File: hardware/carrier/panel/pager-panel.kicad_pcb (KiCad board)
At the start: 2 copper layers, 40 x 20 mm, 27 parts, among them J1 GDEY029T94 FPC, J2 CARRIER, J3 FL-A FPC (FL03), J4 FL-B FPC (Orient), J5 FRONTLIGHT, Q5 SI1308EDL

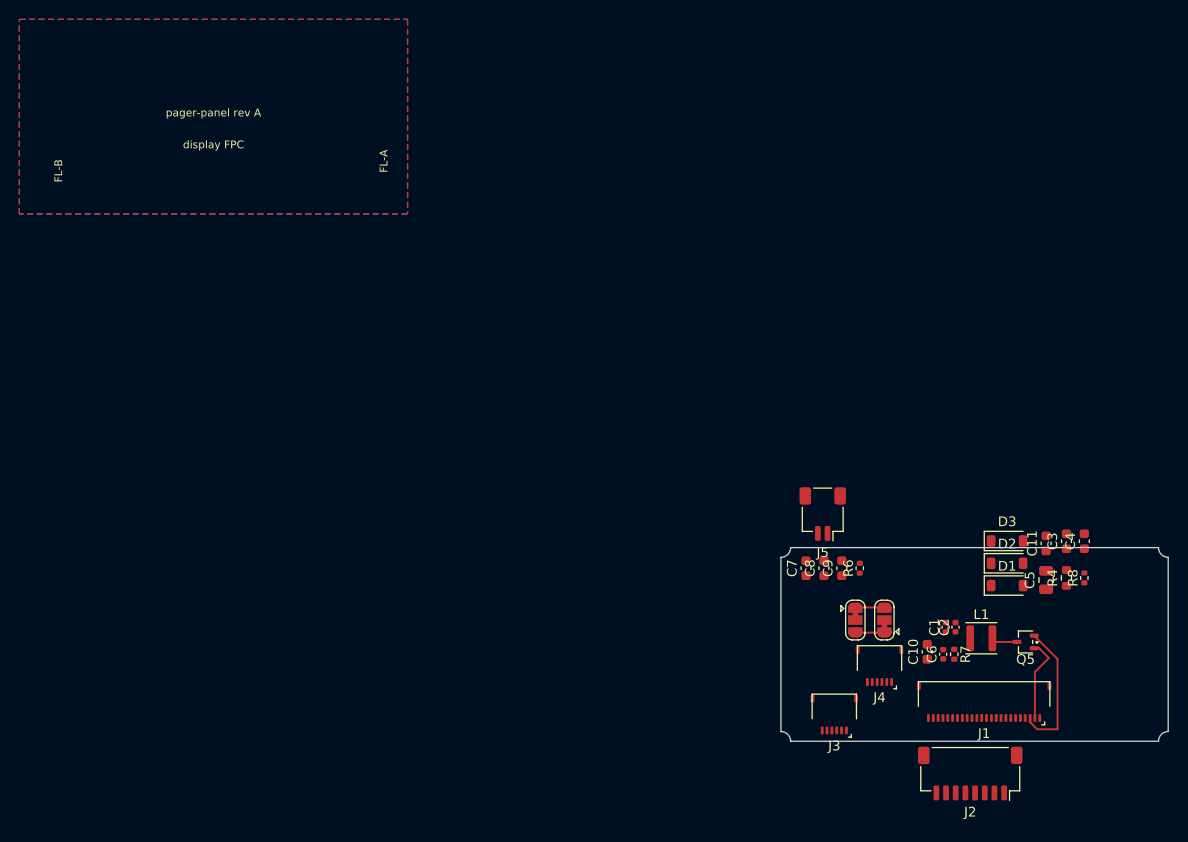
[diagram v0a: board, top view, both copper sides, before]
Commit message: Completed the panel board
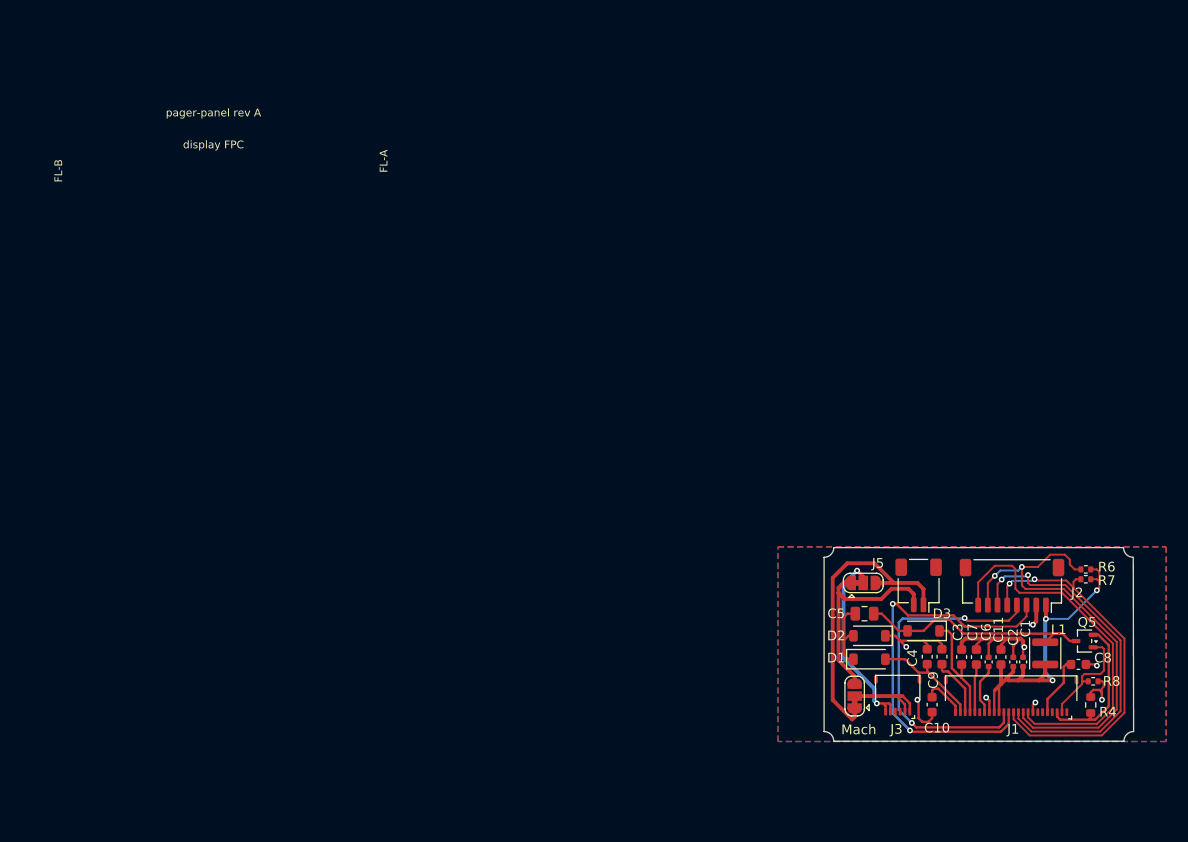
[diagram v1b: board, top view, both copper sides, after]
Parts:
- removed J4: FL-B FPC (Orient), pager-carrier:Hirose_FH34SRJ-6S-0.5SH_1x06-1MP_P0.50mm_Horizontal
- moved C8 28.1 mm to (109.3, 66.6), turned to 0 degrees
- moved R6 23.4 mm to (110.1, 56.8), turned to 180 degrees
- moved C4 20.1 mm to (93.7, 65.8)
- moved J2 19.9 mm to (102.5, 58.5)
- moved C7 19.8 mm to (98.8, 65.8)
- moved C5 19.1 mm to (87.2, 61.3), turned to 180 degrees
- moved C3 16.1 mm to (97.3, 65.8)
- moved D1 16.1 mm to (87.8, 66.0)
- moved D2 16.1 mm to (87.8, 63.6), turned to 180 degrees
- moved R7 15.6 mm to (110.1, 57.8), turned to 180 degrees
- moved C9 13.8 mm to (95.2, 65.8)
- moved R4 13.4 mm to (110.6, 70.8)
- moved D3 12.7 mm to (93.3, 63.1), turned to 180 degrees
- moved C11 12.6 mm to (101.3, 65.8)
- moved J5 12.3 mm to (92.8, 58.4)
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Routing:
- net /panel/EINK_RST: track 0.00 -> 46.6 mm, vias 0 -> 2
- net /panel/EINK_SCK: track 0.00 -> 42.0 mm, vias 0 -> 2
- net /panel/EINK_CS: track 0.00 -> 39.9 mm, vias 0 -> 2
- net GND: track 0.00 -> 39.6 mm, vias 0 -> 8
- net /panel/EINK_DC: track 0.00 -> 38.5 mm, vias 0 -> 2
- net /panel/EINK_BUSY: track 0.00 -> 38.4 mm
- net 3V3_EPD: track 0.00 -> 36.9 mm, vias 0 -> 3
- net /panel/EINK_MOSI: track 0.00 -> 35.5 mm, vias 0 -> 2
- net FL_P: track 3.00 -> 31.3 mm
- net EPD_SW: track 2.69 -> 25.2 mm
- net FL_K: track 0.00 -> 20.4 mm, vias 0 -> 2
- net FL_N: track 3.00 -> 22.2 mm
- net /panel/EPD_VGH: track 0.00 -> 11.6 mm
- net /panel/EPD_VGL: track 0.00 -> 11.4 mm
- net FL_A: track 0.00 -> 8.84 mm
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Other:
- board size 40 x 20 mm -> 32 x 20 mm
- board text added: "CHAM"
- board text added: "Mach"
- board text added: "Panel Board by awongawong"

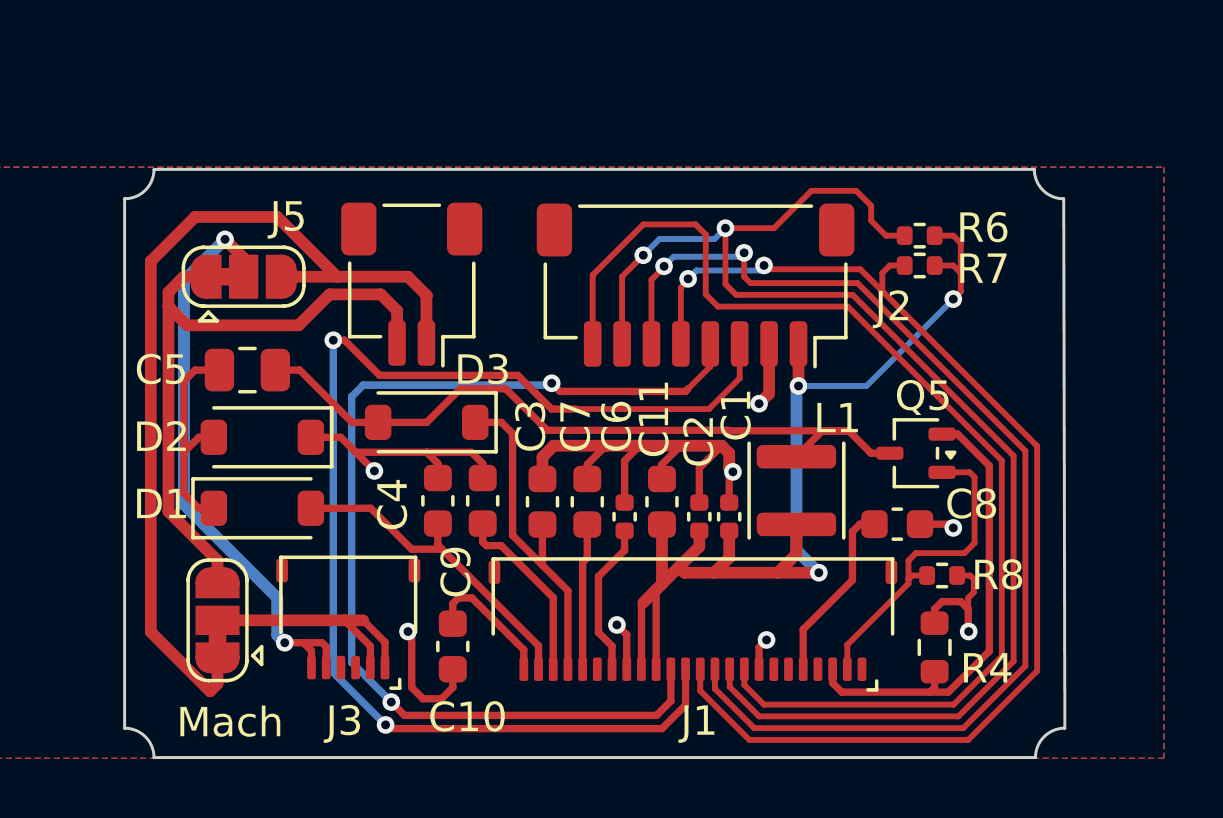
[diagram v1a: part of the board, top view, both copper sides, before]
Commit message: v0.2 boards release candidate
This has almost everything in both boards but we need
a few part swaps.
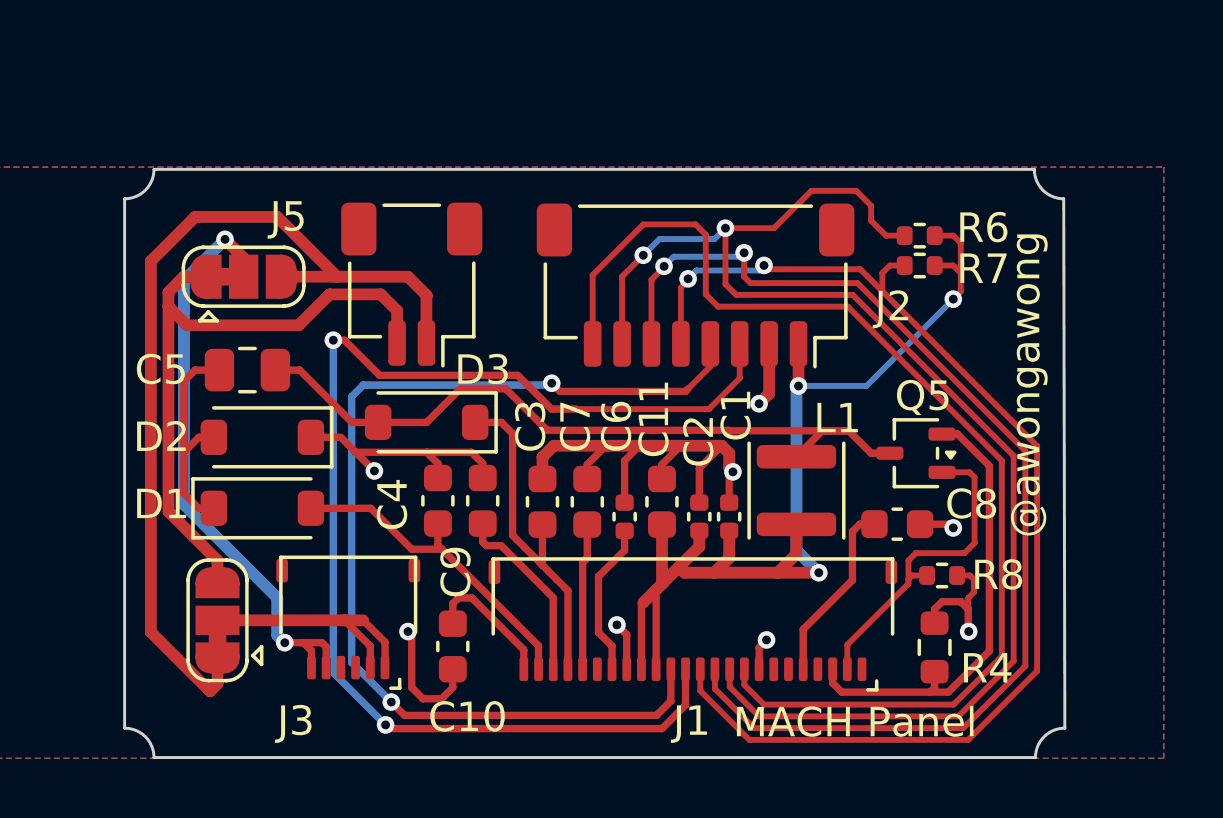
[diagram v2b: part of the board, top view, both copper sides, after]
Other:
- board text added: "@awongawong"
- board text added: "CHAM Panel"
- board text added: "MACH Panel"
- board text removed: "CHAM"
- board text removed: "Mach"
- board text removed: "Panel Board by awongawong"
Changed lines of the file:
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@@
 		(tags "FPC ZIF 0.5mm FH34SRJ Hirose low-profile")
 		(property "Reference" "J1"
-			(at -0.218 -1.766 180)
+			(at 0.036 -1.766 180)
 			(layer "F.SilkS")
 			(effects
@@
 		(tags "FPC ZIF 0.5mm FH34SRJ Hirose low-profile")
 		(property "Reference" "J3"
-			(at 0.127 -1.8215 180)
+			(at 1.778 -1.8215 180)
 			(layer "F.SilkS")
 			(effects
@@
 		)
 	)
-	(gr_text "Mach\n"
-		(at 84.836 73.914 0)
+	(gr_text "MACH Panel"
+		(at 103.759 73.914 0)
 		(layer "F.SilkS")
 		(effects
@@
 		)
 	)
-	(gr_text "Panel Board\nby awongawong"
-		(at 105.156 67.31 0)
+	(gr_text "@awongawong"
+		(at 114.3 67.056 90)
+		(layer "F.SilkS")
+		(effects
+			(font
+				(size 1 1)
+				(thickness 0.1)
+			)
+			(justify left bottom)
+		)
+	)
+	(gr_text "CHAM Panel"
+		(at 113.284 73.914 0)
 		(layer "B.SilkS")
 		(effects
@@
 		)
 	)
-	(gr_text "CHAM"
-		(at 113.284 73.914 0)
+	(gr_text "@awongawong"
+		(at 114.3 56.388 90)
 		(layer "B.SilkS")
 		(effects
